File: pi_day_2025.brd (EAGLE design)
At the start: 50.8 x 25.4 mm, 102 parts, among them IC1 W25Q64JVXGIQ, J4 SM03B-SRSS-TB(LF)(SN), Q2 310mA/60V/1.6Ω, U1 APS6404L-3SQR-ZR, U2 RP2350A, U3 TPS76318DBVRG4, U4 TPS63001DRCR, U5 TXS0108EPWRG4, U6 LSM6DS3TR-C, U7 MCP73833T-AMI/MF, U8 TPS2113APWR, Y1 12MHz

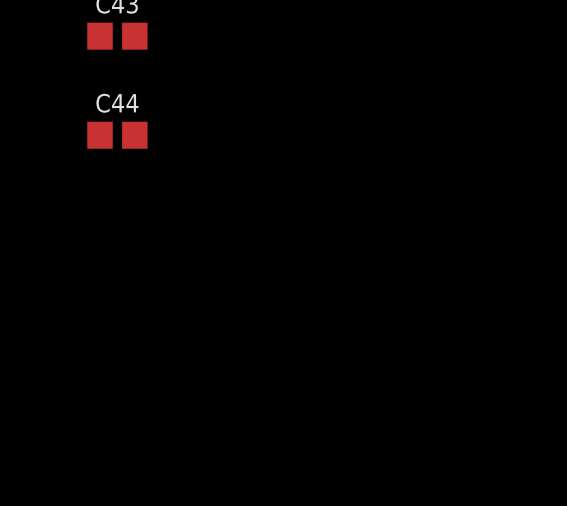
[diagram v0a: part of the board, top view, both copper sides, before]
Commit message: additions to txs0108
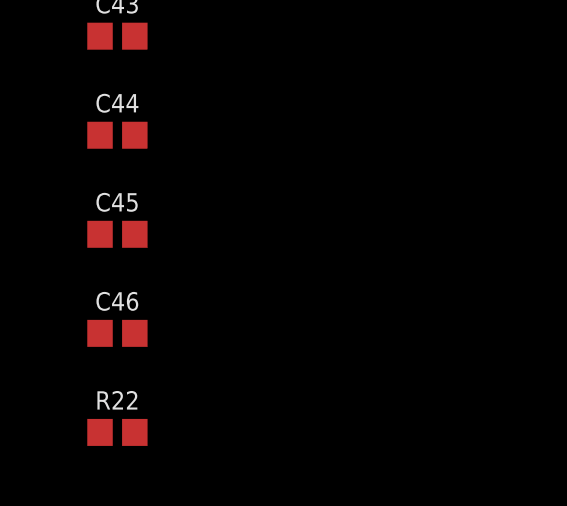
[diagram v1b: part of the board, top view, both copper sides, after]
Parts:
- added C45, C46: 0.1uF, SparkFun-Capacitors:0402
- added R22: 100K, SparkFun-Resistors:0402
- R14: value 500 -> (none)
- R3, R8: value 5.1K -> (none)
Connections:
- removed net VCCA: U5.2
- removed net VCCB: U5.19
- new net N$24: R22.2, U5.10
- net 1.8V: now also C45.2, U5.2
- net 3.3V: now also C46.1, U5.19
- net GND: now also C45.1, C46.2, R22.1
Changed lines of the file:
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@@
 <attribute name="VALUE" x="17.4498" y="24.765" size="0.6096" layer="27" font="vector" ratio="20" rot="R180" align="top-center"/>
 </element>
-<element name="R3" library="SparkFun-Resistors" library_urn="urn:adsk.eagle:library:532" package="0402" package3d_urn="urn:adsk.eagle:package:39657/2" override_package3d_urn="urn:adsk.eagle:package:44163397/2" override_package_urn="urn:adsk.eagle:footprint:39625/1" override_locally_modified="yes" value="5.1K" x="4.2164" y="6.9342" smashed="yes" rot="R90">
+<element name="R3" library="SparkFun-Resistors" library_urn="urn:adsk.eagle:library:532" package="0402" package3d_urn="urn:adsk.eagle:package:39657/2" override_package3d_urn="urn:adsk.eagle:package:44163397/2" override_package_urn="urn:adsk.eagle:footprint:39625/1" override_locally_modified="yes" value=" " x="4.2164" y="6.9342" smashed="yes" rot="R90">
 <attribute name="NAME" x="3.4544" y="6.9342" size="0.6096" layer="25" font="vector" ratio="20" rot="R90" align="bottom-center" display="off"/>
 <attribute name="PROD_ID" value=" " x="4.2164" y="6.9342" size="1.778" layer="27" rot="R90" display="off"/>
@@
 </element>
 <element name="CONN1" library="GT_USB-8012A" package="GT-USB-8012A" override_package3d_urn="urn:adsk.eagle:package:44161671/9" override_package_urn="urn:adsk.eagle:footprint:44161672/1" value="GT-USB_8012A" x="0.0889" y="12.7" smashed="yes" rot="R270"/>
-<element name="R8" library="SparkFun-Resistors" library_urn="urn:adsk.eagle:library:532" package="0402" package3d_urn="urn:adsk.eagle:package:39657/2" override_package3d_urn="urn:adsk.eagle:package:44163391/2" override_package_urn="urn:adsk.eagle:footprint:39625/1" override_locally_modified="yes" value="5.1K" x="1.4478" y="18.6182" smashed="yes" rot="R180">
+<element name="R8" library="SparkFun-Resistors" library_urn="urn:adsk.eagle:library:532" package="0402" package3d_urn="urn:adsk.eagle:package:39657/2" override_package3d_urn="urn:adsk.eagle:package:44163391/2" override_package_urn="urn:adsk.eagle:footprint:39625/1" override_locally_modified="yes" value=" " x="1.4478" y="18.6182" smashed="yes" rot="R180">
 <attribute name="PROD_ID" value=" " x="1.4478" y="18.6182" size="1.778" layer="27" rot="R180" display="off"/>
 <attribute name="VALUE" x="1.4478" y="19.3802" size="0.6096" layer="27" font="vector" ratio="20" rot="R180" align="top-center"/>
@@
 <attribute name="VALUE" value="100K" x="-67.056" y="-219.71" size="0.6096" layer="27" font="vector" ratio="20" align="top-center"/>
 </element>
-<element name="R14" library="SparkFun-Resistors" library_urn="urn:adsk.eagle:library:532" package="0402" package3d_urn="urn:adsk.eagle:package:39657/2" value="500" x="-67.056" y="-222.25" smashed="yes">
+<element name="R14" library="SparkFun-Resistors" library_urn="urn:adsk.eagle:library:532" package="0402" package3d_urn="urn:adsk.eagle:package:39657/2" value=" " x="-67.056" y="-222.25" smashed="yes">
 <attribute name="NAME" x="-67.056" y="-221.488" size="0.6096" layer="25" font="vector" ratio="20" align="bottom-center"/>
 <attribute name="PROD_ID" value=" " x="-67.056" y="-222.25" size="1.778" layer="27" display="off"/>
@@
 <attribute name="PROD_ID" value="CAP-12417" x="-75.692" y="-295.656" size="1.778" layer="27" display="off"/>
 <attribute name="VALUE" x="-75.692" y="-296.418" size="0.6096" layer="27" font="vector" ratio="20" align="top-center"/>
+</element>
+<element name="C45" library="SparkFun-Capacitors" library_urn="urn:adsk.eagle:library:510" package="0402" package3d_urn="urn:adsk.eagle:package:41385089/1" value="0.1uF" x="-75.692" y="-298.958" smashed="yes">
+<attribute name="NAME" x="-75.692" y="-298.196" size="0.6096" layer="25" font="vector" ratio="20" align="bottom-center"/>
+<attribute name="PROD_ID" value="CAP-14993" x="-75.692" y="-298.958" size="1.778" layer="27" display="off"/>
+<attribute name="VALUE" x="-75.692" y="-299.72" size="0.6096" layer="27" font="vector" ratio="20" align="top-center"/>
+</element>
+<element name="C46" library="SparkFun-Capacitors" library_urn="urn:adsk.eagle:library:510" package="0402" package3d_urn="urn:adsk.eagle:package:41385089/1" value="0.1uF" x="-75.692" y="-302.26" smashed="yes">
+<attribute name="NAME" x="-75.692" y="-301.498" size="0.6096" layer="25" font="vector" ratio="20" align="bottom-center"/>
+<attribute name="PROD_ID" value="CAP-14993" x="-75.692" y="-302.26" size="1.778" layer="27" display="off"/>
+<attribute name="VALUE" x="-75.692" y="-303.022" size="0.6096" layer="27" font="vector" ratio="20" align="top-center"/>
+</element>
+<element name="R22" library="SparkFun-Resistors" library_urn="urn:adsk.eagle:library:532" package="0402" package3d_urn="urn:adsk.eagle:package:39657/2" value="100K" x="-75.692" y="-305.562" smashed="yes">
+<attribute name="NAME" x="-75.692" y="-304.8" size="0.6096" layer="25" font="vector" ratio="20" align="bottom-center"/>
+<attribute name="PROD_ID" value="RES-13495" x="-75.692" y="-305.562" size="1.778" layer="27" display="off"/>
+<attribute name="VALUE" x="-75.692" y="-306.324" size="0.6096" layer="27" font="vector" ratio="20" align="top-center"/>
 </element>
 </elements>
@@
 <contactref element="C43" pad="2"/>
 <contactref element="C44" pad="2"/>
+<contactref element="C45" pad="1"/>
+<contactref element="C46" pad="2"/>
+<contactref element="R22" pad="1"/>
 <wire x1="-47.991" y1="-197.104" x2="-50.978" y2="-197.997" width="0" layer="19" extent="1-1"/>
 <wire x1="-54.872" y1="-203.538" x2="-50.978" y2="-197.997" width="0" layer="19" extent="1-1"/>
@@
 <wire x1="-75.112" y1="-292.354" x2="-75.112" y2="-289.052" width="0" layer="19" extent="1-1"/>
 <wire x1="-75.112" y1="-295.656" x2="-75.112" y2="-292.354" width="0" layer="19" extent="1-1"/>
+<wire x1="-76.272" y1="-298.958" x2="-75.112" y2="-295.656" width="0" layer="19" extent="1-1"/>
+<wire x1="-75.112" y1="-302.26" x2="-76.272" y2="-298.958" width="0" layer="19" extent="1-1"/>
+<wire x1="-76.272" y1="-305.562" x2="-75.112" y2="-302.26" width="0" layer="19" extent="1-1"/>
 <wire x1="-16.903" y1="-171.45" x2="-39.869" y2="-197.836" width="0" layer="19" extent="1-1"/>
 <wire x1="-17.708" y1="-157.48" x2="-16.903" y2="-171.45" width="0" layer="19" extent="1-1"/>
@@
 <contactref element="U3" pad="3"/>
 <contactref element="C26" pad="1"/>
+<contactref element="U5" pad="19"/>
+<contactref element="C46" pad="1"/>
 <wire x1="-47.991" y1="-198.054" x2="-47.991" y2="-196.154" width="0" layer="19" extent="1-1"/>
+<wire x1="-50.978" y1="-192.797" x2="-47.991" y2="-196.154" width="0" layer="19" extent="1-1"/>
 <wire x1="-54.872" y1="-201.338" x2="-47.991" y2="-198.054" width="0" layer="19" extent="1-1"/>
 <wire x1="-56.722" y1="-201.688" x2="-54.872" y2="-201.338" width="0" layer="19" extent="1-1"/>
@@
 <wire x1="-76.192" y1="-266.192" x2="-76.192" y2="-263.144" width="0" layer="19" extent="1-1"/>
 <wire x1="-76.272" y1="-289.052" x2="-76.192" y2="-266.192" width="0" layer="19" extent="1-1"/>
+<wire x1="-76.272" y1="-302.26" x2="-76.272" y2="-289.052" width="0" layer="19" extent="1-1"/>
 </signal>
 <signal name="!RESET">
@@
 <contactref element="C25" pad="1"/>
 <contactref element="C43" pad="1"/>
+<contactref element="U5" pad="2"/>
+<contactref element="C45" pad="2"/>
+<wire x1="-45.481" y1="-196.154" x2="-56.718" y2="-192.797" width="0" layer="19" extent="1-1"/>
 <wire x1="-39.869" y1="-195.539" x2="-45.481" y2="-196.154" width="0" layer="19" extent="1-1"/>
 <wire x1="-76.192" y1="-286.004" x2="-45.481" y2="-196.154" width="0" layer="19" extent="1-1"/>
 <wire x1="-76.272" y1="-292.354" x2="-76.192" y2="-286.004" width="0" layer="19" extent="1-1"/>
-</signal>
-<signal name="VCCA">
-<contactref element="U5" pad="2"/>
-</signal>
-<signal name="VCCB">
-<contactref element="U5" pad="19"/>
+<wire x1="-75.112" y1="-298.958" x2="-76.272" y2="-292.354" width="0" layer="19" extent="1-1"/>
 </signal>
 <signal name="NPXL_1_OUT">
@@
 <wire x1="-76.272" y1="-295.656" x2="-40.894" y2="-195.539" width="0" layer="19" extent="1-1"/>
 </signal>
+<signal name="N$24">
+<contactref element="R22" pad="2"/>
+<contactref element="U5" pad="10"/>
+<wire x1="-75.112" y1="-305.562" x2="-56.718" y2="-197.997" width="0" layer="19" extent="1-1"/>
+</signal>
 </signals>

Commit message: Added pinouts for IA611 & voltage level converter
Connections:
- new net IA611_IRQ: U5.17
- new net IA611_IRQ_LP: MK1.6, U5.4
- new net PDM_CLK: U5.20
- new net PDM_CLK_LP: MK1.3, U5.1
- new net PDM_SDO: U5.18
- new net PDM_SDO_LP: MK1.5, U5.3
- new net UART_RX: U5.15
- new net UART_RX_LP: MK1.8, U5.6
- new net UART_TX: U5.16
- new net UART_TX_LP: MK1.9, U5.5
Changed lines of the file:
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@@
 <wire x1="-75.112" y1="-305.562" x2="-56.718" y2="-197.997" width="0" layer="19" extent="1-1"/>
+</signal>
+<signal name="PDM_CLK_LP">
+<contactref element="MK1" pad="3"/>
+<contactref element="U5" pad="1"/>
+<wire x1="-41.919" y1="-195.539" x2="-56.718" y2="-192.147" width="0" layer="19" extent="1-1"/>
+</signal>
+<signal name="PDM_SDO_LP">
+<contactref element="MK1" pad="5"/>
+<contactref element="U5" pad="3"/>
+<wire x1="-40.894" y1="-196.409" x2="-56.718" y2="-193.447" width="0" layer="19" extent="1-1"/>
+</signal>
+<signal name="IA611_IRQ_LP">
+<contactref element="MK1" pad="6"/>
+<contactref element="U5" pad="4"/>
+<wire x1="-41.937" y1="-196.409" x2="-56.718" y2="-194.097" width="0" layer="19" extent="1-1"/>
+</signal>
+<signal name="UART_RX_LP">
+<contactref element="MK1" pad="8"/>
+<contactref element="U5" pad="6"/>
+<wire x1="-40.894" y1="-197.836" x2="-56.718" y2="-195.397" width="0" layer="19" extent="1-1"/>
+</signal>
+<signal name="UART_TX_LP">
+<contactref element="MK1" pad="9"/>
+<contactref element="U5" pad="5"/>
+<wire x1="-41.919" y1="-197.836" x2="-56.718" y2="-194.747" width="0" layer="19" extent="1-1"/>
+</signal>
+<signal name="PDM_CLK">
+<contactref element="U5" pad="20"/>
+</signal>
+<signal name="PDM_SDO">
+<contactref element="U5" pad="18"/>
+</signal>
+<signal name="IA611_IRQ">
+<contactref element="U5" pad="17"/>
+</signal>
+<signal name="UART_TX">
+<contactref element="U5" pad="16"/>
+</signal>
+<signal name="UART_RX">
+<contactref element="U5" pad="15"/>
 </signal>
 </signals>

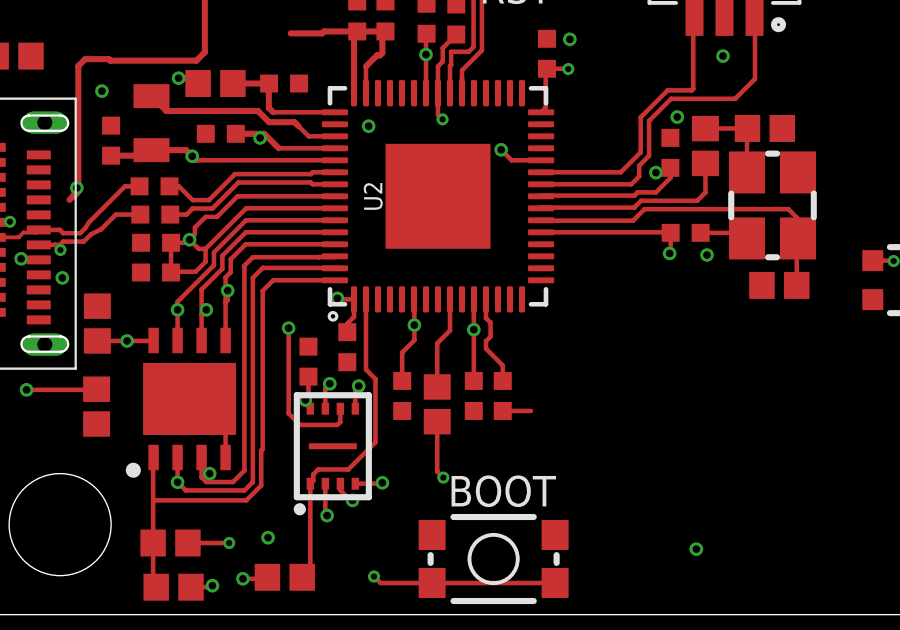
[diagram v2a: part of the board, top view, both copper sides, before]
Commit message: Added PDM microphone
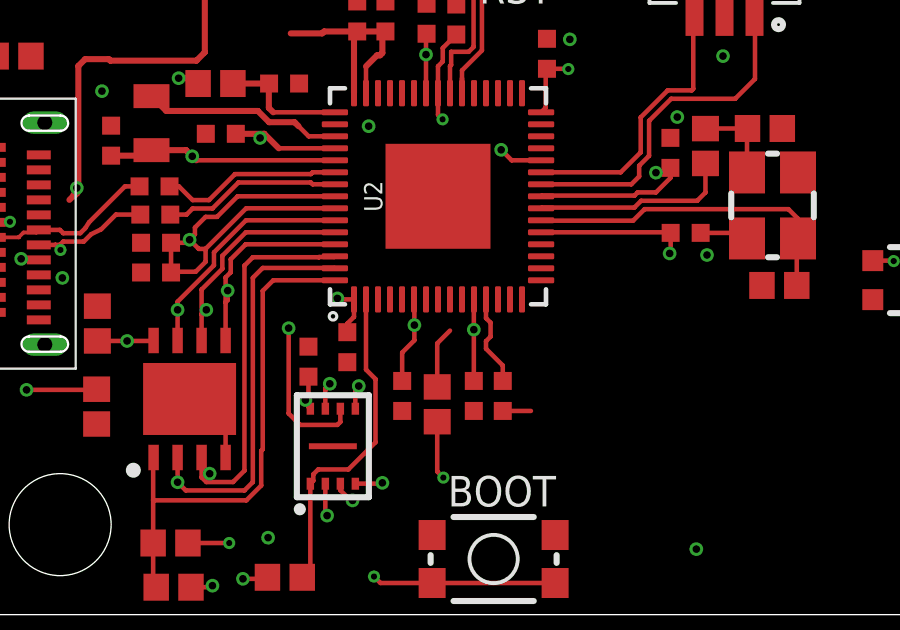
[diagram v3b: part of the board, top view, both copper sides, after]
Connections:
- net BUZZER_DRIVER: now also U2.14; no longer U2.9
- net IA611_IRQ: now also U2.9
- net PDM_CLK: now also U2.5
- net PDM_SDO: now also U2.4
- net UART_RX: now also U2.7
- net UART_TX: now also U2.8
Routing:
- net BUZZER_DRIVER: track 3.09 -> 2.05 mm
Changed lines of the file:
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@@
 </signal>
 <signal name="BUZZER_DRIVER">
-<contactref element="U2" pad="9"/>
 <contactref element="R25" pad="2"/>
-<wire x1="15.9956" y1="10.5081" x2="15.9956" y2="9.4678" width="0.1524" layer="1"/>
 <wire x1="15.9956" y1="9.4678" x2="15.5702" y2="9.0424" width="0.1524" layer="1"/>
 <wire x1="15.5702" y1="9.0424" x2="15.5702" y2="7.5904" width="0.1524" layer="1"/>
+<contactref element="U2" pad="14"/>
+<wire x1="15.9956" y1="9.4678" x2="17.9956" y2="10.5081" width="0" layer="19" extent="1-1"/>
 </signal>
 <signal name="N$26">
@@
 <signal name="PDM_CLK">
 <contactref element="U5" pad="20"/>
+<contactref element="U2" pad="5"/>
+<wire x1="14.3956" y1="10.5081" x2="-50.978" y2="-192.147" width="0" layer="19" extent="1-1"/>
 </signal>
 <signal name="PDM_SDO">
 <contactref element="U5" pad="18"/>
+<contactref element="U2" pad="4"/>
+<wire x1="13.9956" y1="10.5081" x2="-50.978" y2="-193.447" width="0" layer="19" extent="1-1"/>
 </signal>
 <signal name="IA611_IRQ">
 <contactref element="U5" pad="17"/>
+<contactref element="U2" pad="9"/>
+<wire x1="15.9956" y1="10.5081" x2="-50.978" y2="-194.097" width="0" layer="19" extent="1-1"/>
 </signal>
 <signal name="UART_TX">
 <contactref element="U5" pad="16"/>
+<contactref element="U2" pad="8"/>
+<wire x1="15.5956" y1="10.5081" x2="-50.978" y2="-194.747" width="0" layer="19" extent="1-1"/>
 </signal>
 <signal name="UART_RX">
 <contactref element="U5" pad="15"/>
+<contactref element="U2" pad="7"/>
+<wire x1="15.1956" y1="10.5081" x2="-50.978" y2="-195.397" width="0" layer="19" extent="1-1"/>
 </signal>
 </signals>

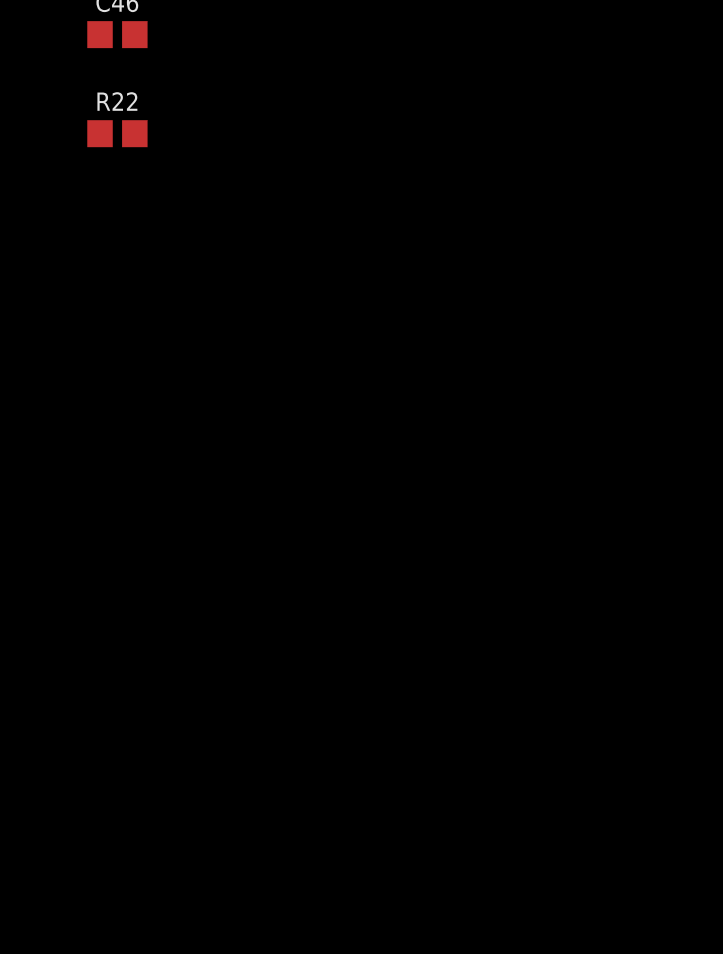
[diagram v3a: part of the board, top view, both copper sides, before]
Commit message: Added ESP32 chipset.
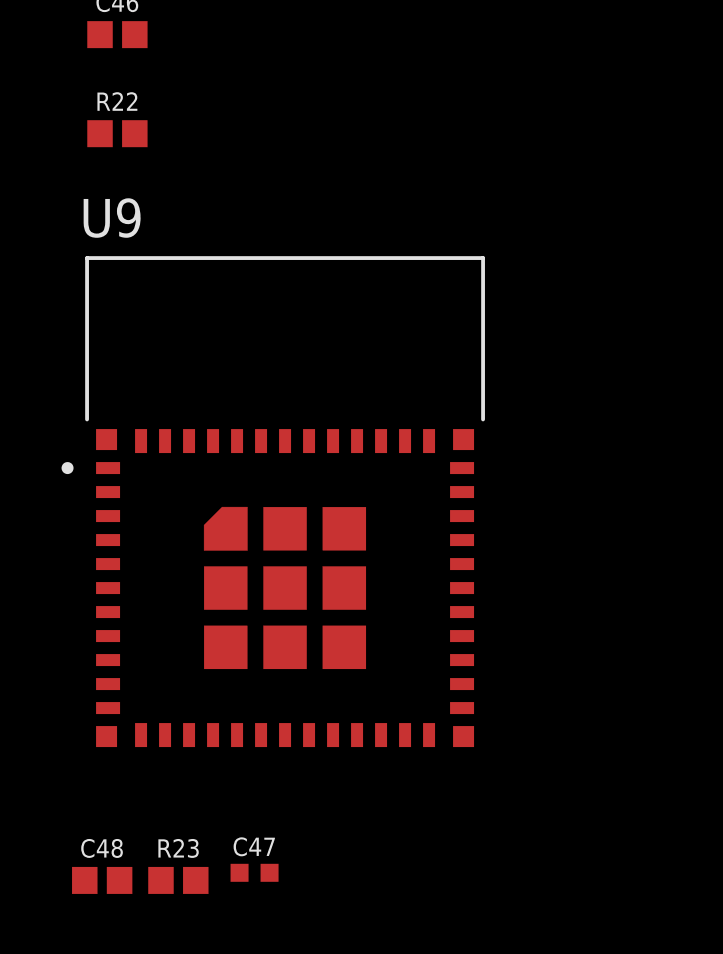
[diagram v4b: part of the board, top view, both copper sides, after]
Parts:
- added C47: 10uF, SparkFun-Capacitors:0402-TIGHT
- added C48: 0.1uF, SparkFun-Capacitors:0402
- added R23: 10k, SparkFun-Resistors:0402
- added U9: ESP32-C3-MINI-1-N4, ESP32-C3-MINI-1-N4:XCVR_ESP32-C3-MINI-1-N4
- R10, R11, R14, R15, R20, R22, R3, R4, R5, R6, R7, R8, R9: device SparkFun-Resistors:0402 -> SparkFun-Resistors:0402@1
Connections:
- new net !ESP32_BOOT: U2.31, U9.23
- new net !ESP32_RST: U2.29, U9.8
- new net ESP32_CS: U2.33, U9.16
- new net ESP32_HANDSHAKE: U2.28, U9.6
- new net ESP32_MISO: U2.32, U9.5
- new net ESP32_MOSI: U2.35, U9.21
- new net ESP32_RX: U2.16, U9.30
- new net ESP32_SCK: U2.34, U9.20
- new net ESP32_TX: U2.17, U9.31
- new net N$25: R23.1, U9.22
- net 3.3V: now also C47.1, C48.1, R23.2, U9.3
- net GND: now also C47.2, C48.2, U9.1, U9.11, U9.14, U9.2, U9.36, U9.37, U9.38, U9.39, U9.40, U9.41, U9.42, U9.43, U9.44, U9.45, U9.46, U9.47, U9.48, U9.49_1, U9.49_2, U9.49_3, U9.49_4, U9.49_5, U9.49_6, U9.49_7, U9.49_8, U9.49_9, U9.50, U9.51, U9.52, U9.53
- net LSM6_INT1: now also U2.19
- net LSM6_INT2: now also U2.27

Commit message: COmpleted schematic
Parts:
- CONN1: value GT-USB_8012A -> TYPE-C-31-M-12; device GT_USB-8012A:GT-USB-8012A -> TYPE-C-31-M-12:HRO_TYPE-C-31-M-12
- R14: value (none) -> 499
- R3, R8: value (none) -> 5.1K
- R4: value (none) -> DNF
- R5: value (none) -> 1K
- R6, R7: value (none) -> 2.2K
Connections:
- net GND: now also CONN1.A1_B12, CONN1.B1_A12, CONN1.S1, CONN1.S2, CONN1.S3, CONN1.S4; no longer CONN1.A1, CONN1.A12, CONN1.B1, CONN1.B12, CONN1.TH1, CONN1.TH2
- net VBUS: now also CONN1.A4_B9, CONN1.B4_A9; no longer CONN1.A4, CONN1.A9, CONN1.B4, CONN1.B9
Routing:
- net USB_N: track 5.87 -> 15.7 mm
- net USB_P: track 6.63 -> 12.3 mm
- net N$7: track 5.43 -> 10.2 mm
- net N$3: track 7.62 -> 10.8 mm
